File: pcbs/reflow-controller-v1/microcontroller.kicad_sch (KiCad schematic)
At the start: 15 parts, among them J3 SWD, J4 UART, U3 STM32G474VETx

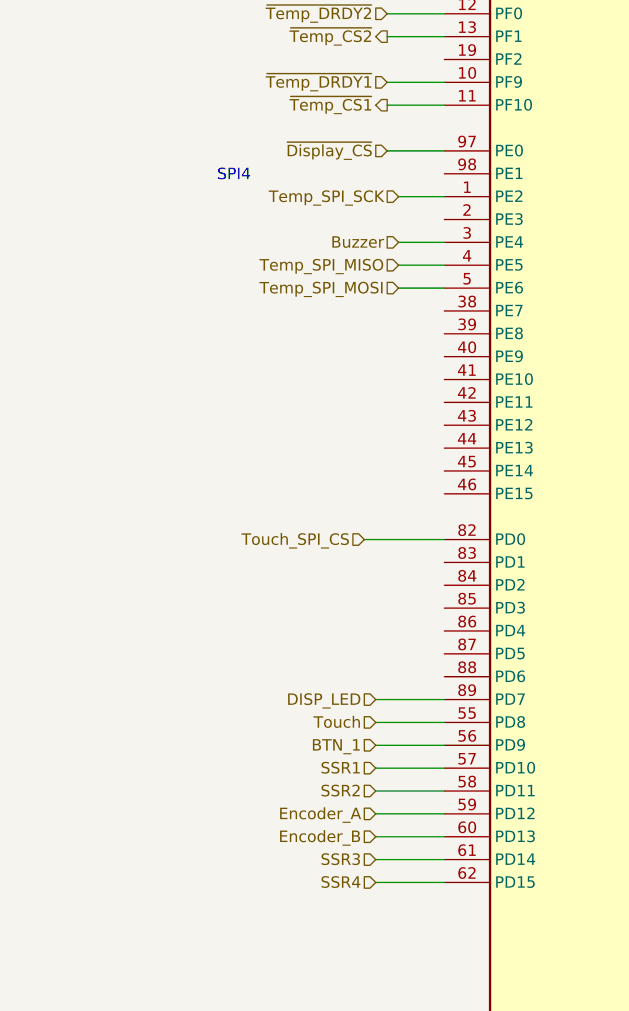
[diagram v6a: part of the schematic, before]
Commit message: add labels to specify encoder periferal
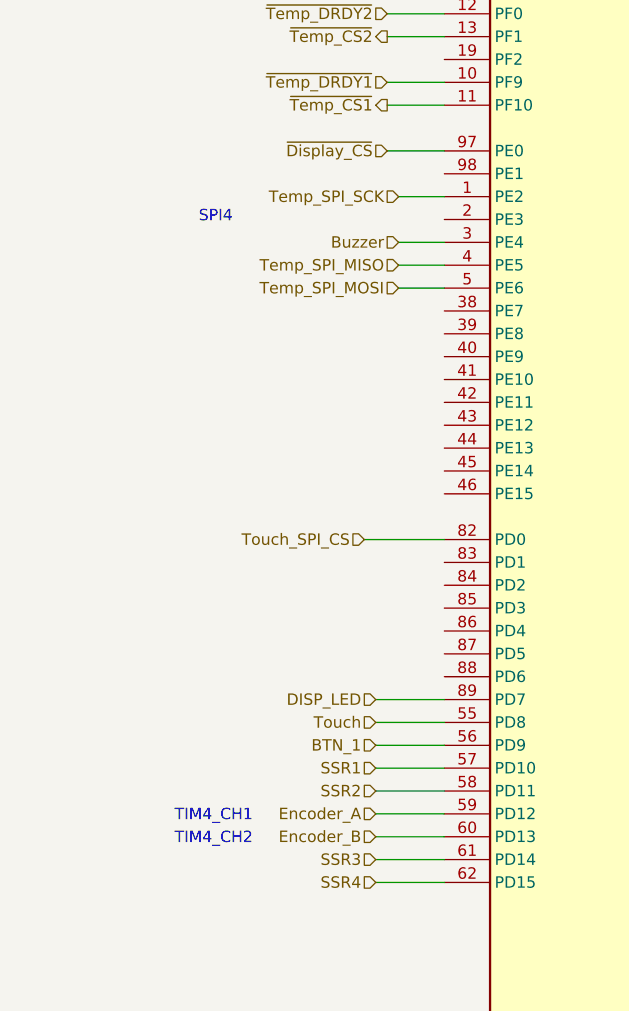
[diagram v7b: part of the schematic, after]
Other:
- note added: "TIM4_CH1"
- note added: "TIM4_CH2"
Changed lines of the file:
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@@
 	(text "SPI4"
 		(exclude_from_sim no)
-		(at 78.232 67.564 0)
+		(at 76.2 72.136 0)
 		(effects
 			(font
@@
 		(exclude_from_sim no)
 		(at 156.972 125.984 0)
+		(effects
+			(font
+				(size 1.27 1.27)
+			)
+			(justify left)
+		)
+	)
+	(text "TIM4_CH2"
+		(exclude_from_sim no)
+		(at 71.628 141.224 0)
 		(effects
 			(font
@@
 		)
 	)
+	(text "TIM4_CH1"
+		(exclude_from_sim no)
+		(at 71.628 138.684 0)
+		(effects
+			(font
+				(size 1.27 1.27)
+			)
+			(justify left)
+		)
+	)

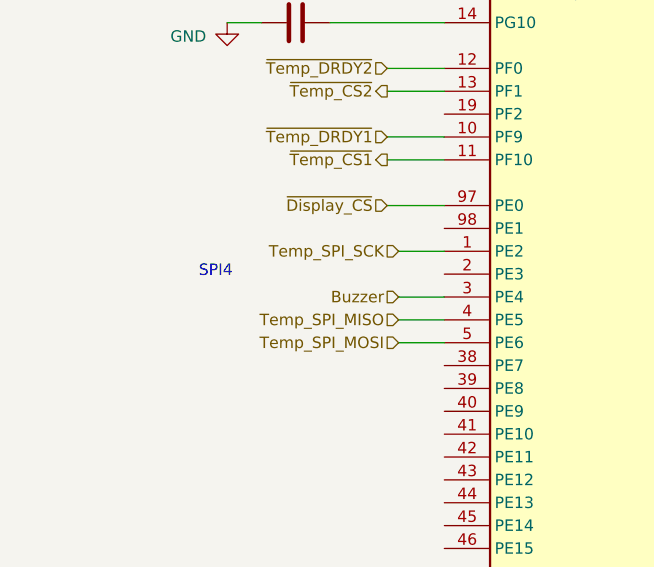
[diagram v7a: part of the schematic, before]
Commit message: add labels to specify buzzer periferal
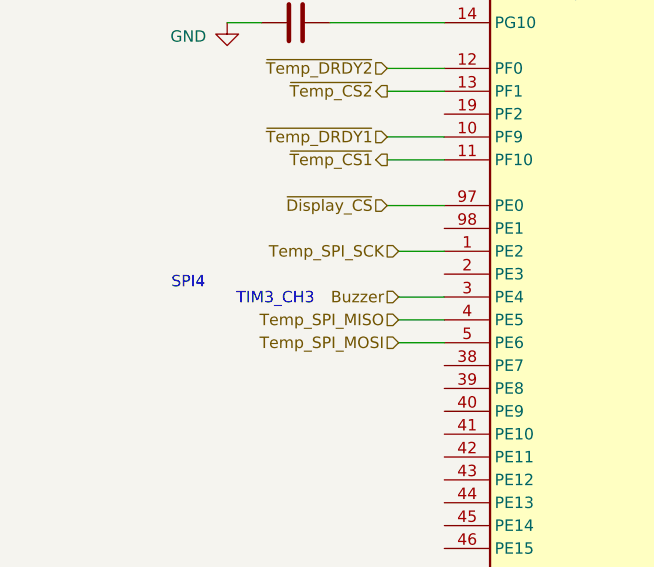
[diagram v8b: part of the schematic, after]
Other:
- note added: "TIM3_CH3"
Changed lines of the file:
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@@
 	(text "SPI4"
 		(exclude_from_sim no)
-		(at 76.2 72.136 0)
+		(at 73.152 73.406 0)
 		(effects
 			(font
@@
 		)
 	)
+	(text "TIM3_CH3"
+		(exclude_from_sim no)
+		(at 78.486 75.184 0)
+		(effects
+			(font
+				(size 1.27 1.27)
+			)
+			(justify left)
+		)
+	)
